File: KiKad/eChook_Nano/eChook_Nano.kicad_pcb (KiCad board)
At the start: 2 copper layers, 75 x 75 mm, 55 parts, among them J1 Expansion, Q1 BC547, U1 Arduino_Nano_v3.x, U2 TSR_1-2450, U3 MCP6002-xP

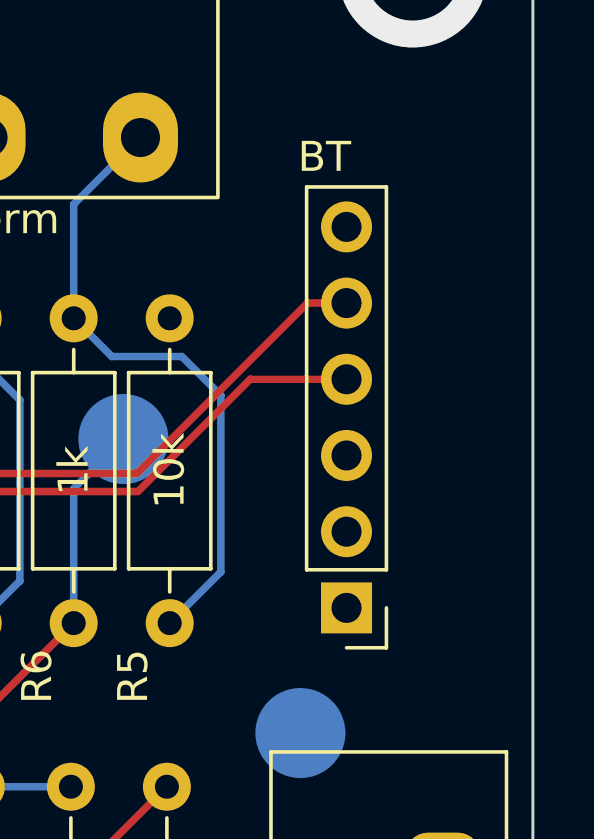
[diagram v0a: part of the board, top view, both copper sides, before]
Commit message: R15 and R24 Value Correction, new IBOM
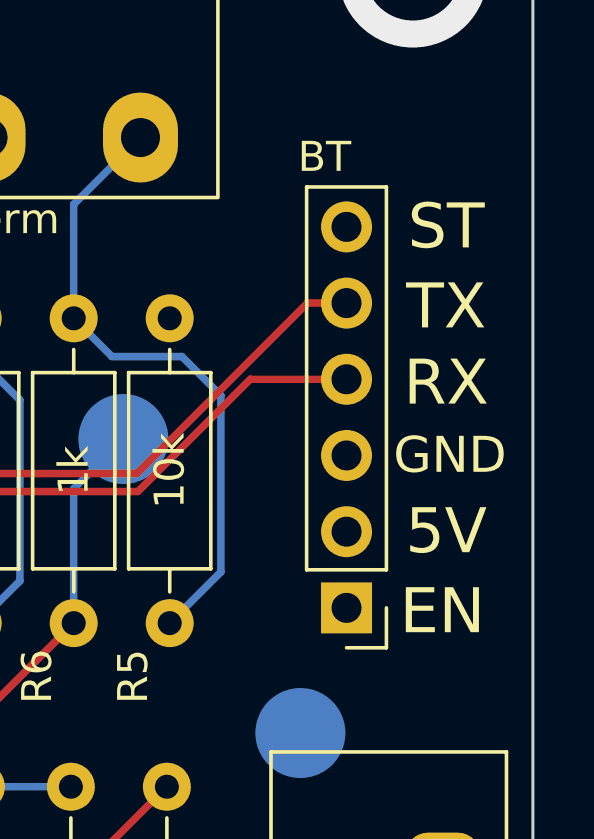
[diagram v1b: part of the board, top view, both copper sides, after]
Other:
- board text added: "5V"
- board text added: "EN"
- board text added: "RX"
- board text added: "ST"
- board text added: "TX"
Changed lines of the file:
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@@
     (effects (font (size 0.9 0.9) (thickness 0.225)) (justify mirror))
+  )
+  (gr_text "ST" (at 181.61 74.168) (layer "F.SilkS")
+    (effects (font (size 1.5 1.5) (thickness 0.3)))
+  )
+  (gr_text "GND" (at 181.737 81.788) (layer "F.SilkS")
+    (effects (font (size 1.2 1.2) (thickness 0.2)))
+  )
+  (gr_text "RX" (at 181.61 79.375) (layer "F.SilkS")
+    (effects (font (size 1.5 1.5) (thickness 0.3)))
   )
   (gr_text "8" (at 111.2 107.2) (layer "F.SilkS")
     (effects (font (size 1 1) (thickness 0.2)))
   )
+  (gr_text "EN" (at 181.483 86.995) (layer "F.SilkS")
+    (effects (font (size 1.5 1.5) (thickness 0.3)))
+  )
   (gr_text "1" (at 130.5 101.2) (layer "F.SilkS")
     (effects (font (size 1 1) (thickness 0.2)))
+  )
+  (gr_text "5V" (at 181.61 84.328) (layer "F.SilkS")
+    (effects (font (size 1.5 1.5) (thickness 0.3)))
+  )
+  (gr_text "TX" (at 181.61 76.835) (layer "F.SilkS")
+    (effects (font (size 1.5 1.5) (thickness 0.3)))
   )
   (gr_text "14\n" (at 130.5 107.2) (layer "F.SilkS")
@@
   (segment (start 120.3 100.8) (end 120.3 84.9) (width 0.25) (layer "F.Cu") (net 17))
   (segment (start 120.98 101.48) (end 120.3 100.8) (width 0.25) (layer "F.Cu") (net 17))
+  (segment (start 117.8 84.86) (end 119.07 83.59) (width 0.25) (layer "F.Cu") (net 18))
   (segment (start 118.44 102.8) (end 118.44 101.54) (width 0.25) (layer "F.Cu") (net 18))
-  (segment (start 117.8 84.86) (end 119.07 83.59) (width 0.25) (layer "F.Cu") (net 18))
   (segment (start 117.8 100.9) (end 117.8 84.86) (width 0.25) (layer "F.Cu") (net 18))
   (segment (start 118.44 101.54) (end 117.8 100.9) (width 0.25) (layer "F.Cu") (net 18))

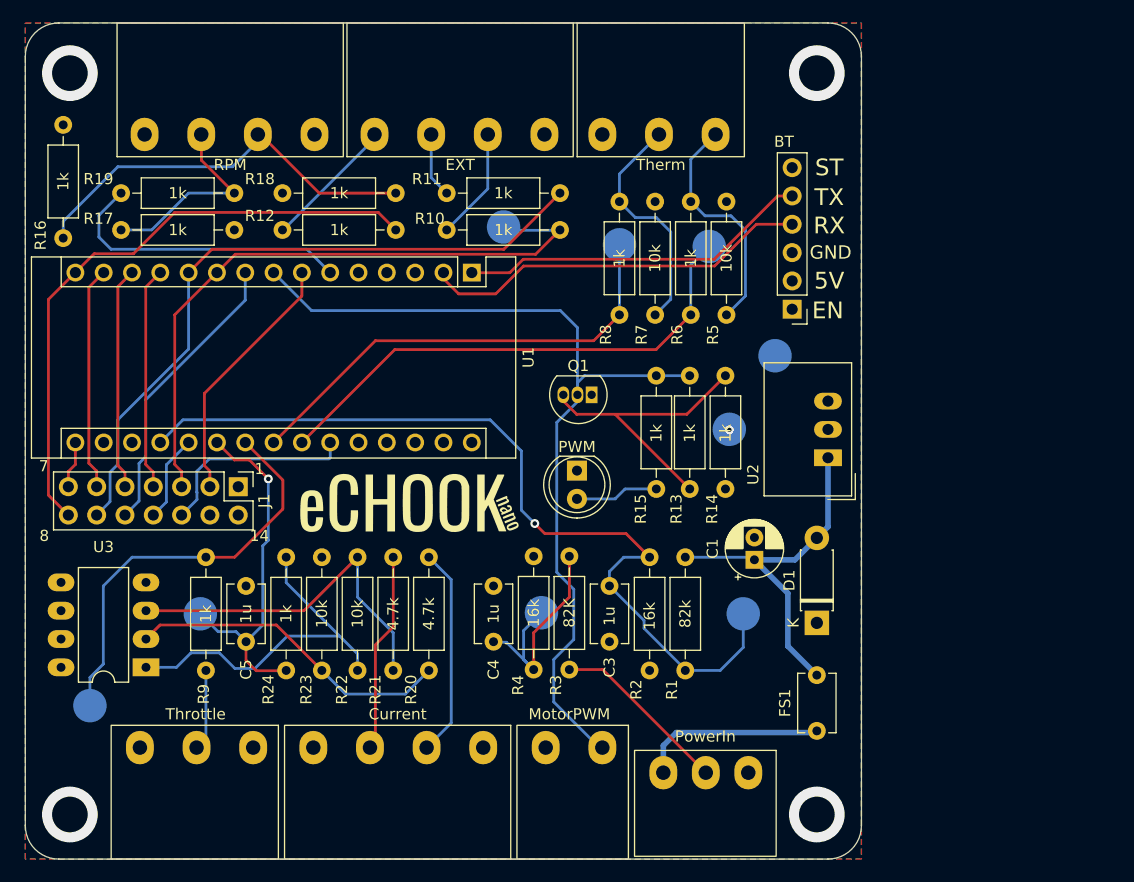
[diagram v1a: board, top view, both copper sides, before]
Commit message: SMD Conversion
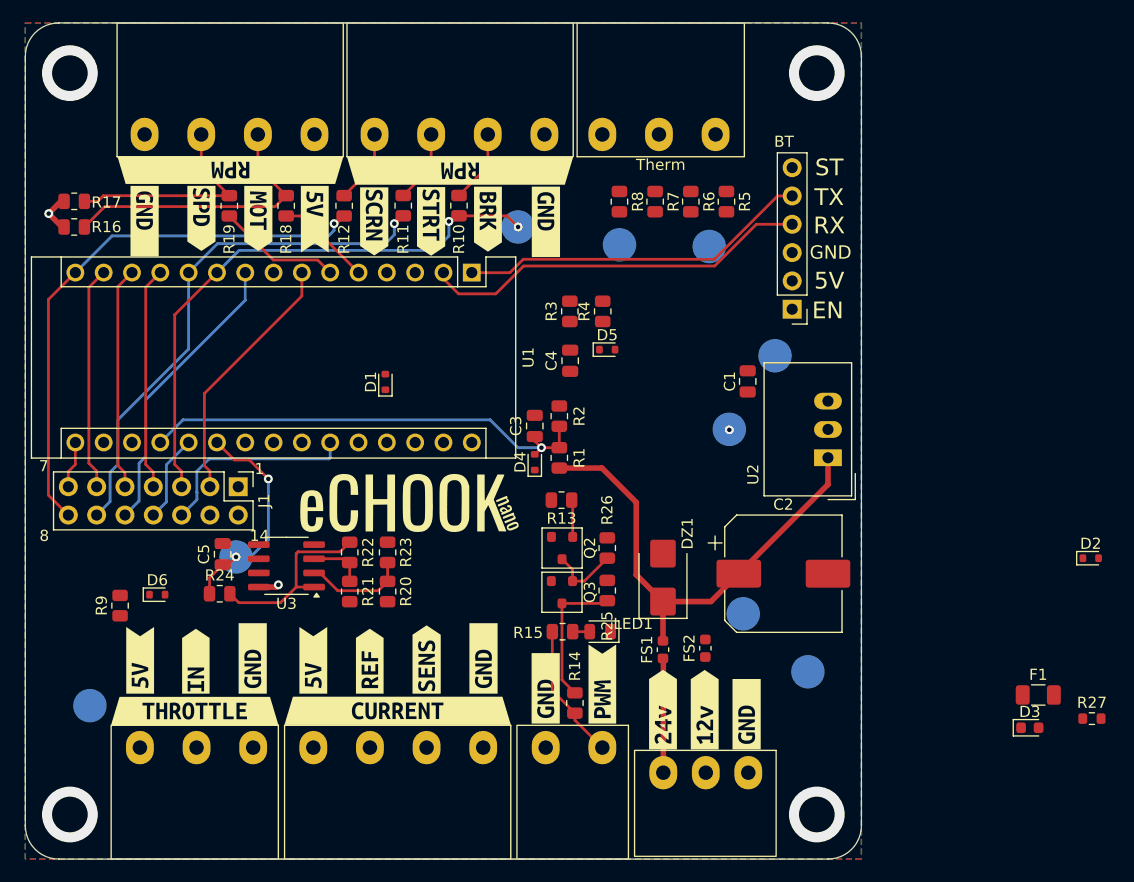
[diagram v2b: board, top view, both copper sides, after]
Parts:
- removed Q1: BC547, Package_TO_SOT_THT:TO-92L_Inline
- added C2: 47uf 63V, Capacitor_SMD:CP_Elec_10x10, F.Cu at (177.5, 110.6)
- added D2: SBD, Diode_SMD:D_SOD-523, F.Cu at (205.1, 109.2)
- added D3: LED, LED_SMD:LED_0603_1608Metric, F.Cu at (199.6, 124.4)
- added D4: SBD, Diode_SMD:D_SOD-523, F.Cu at (155.2, 100.6)
- added D5: SBD, Diode_SMD:D_SOD-523, F.Cu at (161.7, 90.5)
- added D6: SBD, Diode_SMD:D_SOD-523, F.Cu at (121.3, 112.5)
- added DZ1: 33v 35v 37v, Diode_SMD:D_SMB, F.Cu at (166.7, 111.0)
- added F1: Polyfuse, Fuse:Fuse_1206_3216Metric, F.Cu at (200.4, 121.5)
- added FS2: Polyfuse 300mA, Fuse:Fuse_0603_1608Metric, F.Cu at (170.5, 117.3)
- added Q2: Q_NMOS-D_Generic_GSD, PCM_Package_TO_SOT_SMD_AKL:SOT-23, F.Cu at (157.7, 108.3)
- added Q3: Q_NMOS-D_Generic_GSD, PCM_Package_TO_SOT_SMD_AKL:SOT-23, F.Cu at (157.6, 112.3)
- added R25: 10k, Resistor_SMD:R_0805_2012Metric, F.Cu at (161.7, 112.1)
- added R26: 10k, Resistor_SMD:R_0805_2012Metric, F.Cu at (161.7, 108.3)
- added R27: 3.3k 0.1%, Resistor_SMD:R_0603_1608Metric, F.Cu at (205.2, 123.6)
- added kibuzzard-66D71FF8: G***, kibuzzard-66D71FF8, F.Cu at (166.7, 122.8)
- added kibuzzard-66D7200F: G***, kibuzzard-66D7200F, F.Cu at (170.4, 122.8)
- added kibuzzard-66D72019: G***, kibuzzard-66D72019, F.Cu at (156.2, 79.0)
- added kibuzzard-66D72019: G***, kibuzzard-66D72019, F.Cu at (156.2, 120.9)
- added kibuzzard-66D72019: G***, kibuzzard-66D72019, F.Cu at (150.6, 118.2)
- added kibuzzard-66D72019: G***, kibuzzard-66D72019, F.Cu at (129.9, 118.2)
- added kibuzzard-66D72019: G***, kibuzzard-66D72019, F.Cu at (174.2, 123.2)
- added kibuzzard-66D72019: G***, kibuzzard-66D72019, F.Cu at (120.2, 79.0)
- added kibuzzard-66D72322: G***, kibuzzard-66D72322, F.Cu at (161.3, 120.5)
- added kibuzzard-66D72613: G***, kibuzzard-66D72613, F.Cu at (135.3, 118.4)
- added kibuzzard-66D72613: G***, kibuzzard-66D72613, F.Cu at (119.8, 118.4)
- added kibuzzard-66D72613: G***, kibuzzard-66D72613, F.Cu at (135.5, 78.8)
- added kibuzzard-66D727FC: G***, kibuzzard-66D727FC, F.Cu at (140.4, 118.4)
- added kibuzzard-66D7283F: G***, kibuzzard-66D7283F, F.Cu at (145.5, 118.3)
- added kibuzzard-66D728C6: G***, kibuzzard-66D728C6, F.Cu at (124.8, 118.5)
- added kibuzzard-66D728F7: G***, kibuzzard-66D728F7, F.Cu at (124.7, 122.9)
- added kibuzzard-66D72997: G***, kibuzzard-66D72997, F.Cu at (142.9, 122.9)
- added kibuzzard-66D72A35: G***, kibuzzard-66D72A35, F.Cu at (127.9, 74.4)
- added kibuzzard-66D72A35: G***, kibuzzard-66D72A35, F.Cu at (148.5, 74.5)
- added kibuzzard-66D72A68: G***, kibuzzard-66D72A68, F.Cu at (125.3, 78.7)
- added kibuzzard-66D72A7D: G***, kibuzzard-66D72A7D, F.Cu at (130.4, 78.7)
- added kibuzzard-66D72AFE: G***, kibuzzard-66D72AFE, F.Cu at (151.0, 78.8)
- added kibuzzard-66D72B0C: G***, kibuzzard-66D72B0C, F.Cu at (145.9, 79.0)
- added kibuzzard-66D72B26: G***, kibuzzard-66D72B26, F.Cu at (140.8, 79.0)
- C1: value C_Polarized -> 22u 10V; footprint Capacitor_THT:CP_Radial_D5.0mm_P2.00mm -> Capacitor_SMD:C_0805_2012Metric
- C3, C4, C5: footprint Capacitor_THT:C_Disc_D5.1mm_W3.2mm_P5.00mm -> Capacitor_SMD:C_0805_2012Metric
- D1: value DIODE -> SBD; footprint Diode_THT:D_DO-41_SOD81_P7.62mm_Horizontal -> Diode_SMD:D_SOD-523
- FS1: value Polyfuse -> Polyfuse 300mA; footprint Capacitor_THT:C_Disc_D5.1mm_W3.2mm_P5.00mm -> Fuse:Fuse_0603_1608Metric
- LED1: renamed from PWM1; value PWM -> LED_GREEN; footprint LED_THT:LED_D5.0mm -> LED_SMD:LED_0805_2012Metric
- R1, R10, R11, R12, R14, R18, R19, R2, R20, R21, R22, R23, R3, R4, R5, R6, R7, R8, R9: footprint Resistor_THT:R_Axial_DIN0207_L6.3mm_D2.5mm_P10.16mm_Horizontal -> Resistor_SMD:R_0805_2012Metric
- R13, R15, R16, R17, R24: value 1k -> 10k; footprint Resistor_THT:R_Axial_DIN0207_L6.3mm_D2.5mm_P10.16mm_Horizontal -> Resistor_SMD:R_0805_2012Metric
- U3: footprint Package_DIP:DIP-8_W7.62mm_LongPads -> Package_SO:SOIC-8_3.9x4.9mm_P1.27mm
- moved D1 44.3 mm to (141.8, 93.4)
- moved R4 32.7 mm to (161.3, 87.1)
- moved R3 32.1 mm to (158.3, 87.1)
- moved R14 31.1 mm to (158.8, 122.2), turned to 90 degrees
- moved C4 26.1 mm to (158.4, 91.5)
- moved TP2 24.5 mm to (179.7, 119.4)
- moved C1 16.0 mm to (174.3, 93.3), turned to -90 degrees
- moved C3 15.8 mm to (155.2, 97.3), turned to 90 degrees
- moved FS1 15.6 mm to (166.7, 117.4)
- moved U3 15.5 mm to (132.9, 109.9)
- moved R15 15.3 mm to (157.7, 115.8), turned to 180 degrees
- moved R2 15.0 mm to (157.4, 96.5), turned to 90 degrees
- moved R13 14.7 mm to (157.6, 104.0), turned to 180 degrees
- moved LED1 14.6 mm to (161.1, 115.8), turned to 180 degrees
- moved R1 14.4 mm to (157.4, 100.2), turned to 90 degrees
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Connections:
- C1 pad 1: +24V -> +5V
- Conn2 pad 2: +12V -> Net-(Conn2-Pin_2)
- Conn8 pad 2: /MotorPWM -> Net-(Conn8-Pin_2)
- D1 pad 1: GND -> +5V
- D1 pad 2: +24V -> /Temp2
- R13 pad 1: GND -> /MotorPWM
- R13 pad 2: Net-(Q1-Pad3) -> GND
- R14 pad 1: /MotorPWM -> Net-(Conn8-Pin_2)
- R14 pad 2: Net-(Q1-Pad3) -> Net-(Q3-D)
- R15 pad 2: /MotorPWM -> Net-(Conn8-Pin_2)
- R18 pad 1: /MotorRMP -> /MotorRPM
- R20 pad 1: Net-(R20-Pad1) -> Net-(U3A--)
- R23 pad 1: Net-(R20-Pad1) -> GND
- R23 pad 2: GND -> Net-(U3A--)
- U3 pad 2: Net-(R20-Pad1) -> Net-(U3A--)
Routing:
- net /MotorPWM: track 81.6 -> 3.34 mm
- net /Temp1: track 46.4 -> 0.00 mm
- net /Temp2: track 40.8 -> 0.00 mm
- net /Throttle: track 37.6 -> 0.00 mm
- net /BattTotalV: track 77.8 -> 41.7 mm
- net Net-(R20-Pad1): track 29.3 -> 0.00 mm
- net Net-(U3A-+): track 32.4 -> 5.03 mm
- net Net-(Q1-Pad3): track 25.9 -> 0.00 mm
- net /Batt1v: track 22.4 -> 0.00 mm
- net Net-(Conn3-Pin_2): track 21.2 -> 0.00 mm
- net Net-(Conn3-Pin_1): track 21.2 -> 0.00 mm
- net Net-(Conn1-Pin_3): track 18.8 -> 0.00 mm
- net Net-(Conn1-Pin_2): track 17.3 -> 0.00 mm
- net +12V: track 16.1 -> 0.00 mm
- net Net-(R22-Pad1): track 32.5 -> 16.7 mm
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
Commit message: Routing Complete
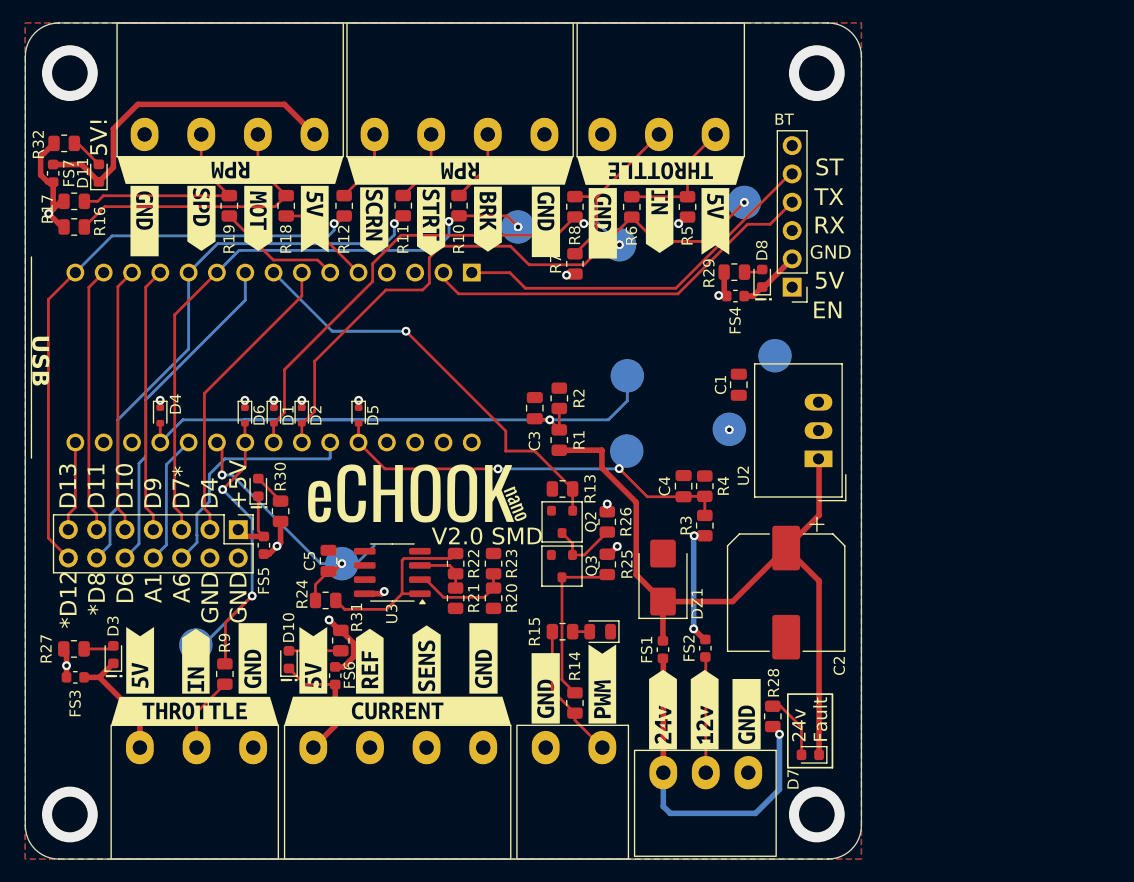
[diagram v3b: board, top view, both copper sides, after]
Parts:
- removed F1: Polyfuse, Fuse:Fuse_1206_3216Metric
- added BC1: BOM-Component, eChook:BOM-Component, F.Cu at (112.2, 83.7)
- added BC2: BOM-Component, eChook:BOM-Component, F.Cu at (112.2, 99.1)
- added D10: LED, LED_SMD:LED_0603_1608Metric, F.Cu at (133.2, 118.3)
- added D11: LED, LED_SMD:LED_0603_1608Metric, F.Cu at (116.1, 74.7)
- added D7: LED, LED_SMD:LED_0603_1608Metric, F.Cu at (179.9, 126.8)
- added D8: LED, LED_SMD:LED_0603_1608Metric, F.Cu at (175.6, 84.1)
- added D9: LED, LED_SMD:LED_0603_1608Metric, F.Cu at (130.4, 102.9)
- added FS3: Polyfuse 300mA, Fuse:Fuse_0603_1608Metric, F.Cu at (114.0, 119.9)
- added FS4: Polyfuse 300mA, Fuse:Fuse_0603_1608Metric, F.Cu at (173.2, 85.7)
- added FS5: Polyfuse 300mA, Fuse:Fuse_0603_1608Metric, F.Cu at (130.9, 108.0)
- added FS6: Polyfuse 300mA, Fuse:Fuse_0603_1608Metric, F.Cu at (137.3, 119.8)
- added FS7: Polyfuse 300mA, Fuse:Fuse_0603_1608Metric, F.Cu at (112.0, 74.7)
- added R28: 10k, Resistor_SMD:R_0805_2012Metric, F.Cu at (176.6, 123.4)
- added R29: 1k, Resistor_SMD:R_0805_2012Metric, F.Cu at (173.1, 83.5)
- added R30: 1k, Resistor_SMD:R_0805_2012Metric, F.Cu at (132.4, 105.0)
- added R31: 1k, Resistor_SMD:R_0805_2012Metric, F.Cu at (137.8, 116.6)
- added R32: 1k, Resistor_SMD:R_0805_2012Metric, F.Cu at (113.0, 72.0)
- added kibuzzard-66D72019: G***, kibuzzard-66D72019, F.Cu at (161.3, 79.2)
- added kibuzzard-66D72613: G***, kibuzzard-66D72613, F.Cu at (171.4, 79.0)
- added kibuzzard-66D728C6: G***, kibuzzard-66D728C6, F.Cu at (166.4, 78.9)
- added kibuzzard-66D728F7: G***, kibuzzard-66D728F7, F.Cu at (166.5, 74.5)
- R27: value 3.3k 0.1% -> 1k; footprint Resistor_SMD:R_0603_1608Metric -> Resistor_SMD:R_0805_2012Metric
- moved R27 91.5 mm to (113.9, 117.3), turned to 180 degrees
- moved D3 82.5 mm to (117.4, 117.9), turned to 90 degrees
- moved D2 71.9 mm to (134.3, 96.4), turned to -90 degrees
- moved G*** 67.6 mm to (79.9, 49.3)
- moved D4 33.9 mm to (121.6, 96.4), turned to -90 degrees
- moved TP2 25.6 mm to (163.4, 99.6)
- moved TP1 23.7 mm to (163.5, 92.8)
- moved D5 23.1 mm to (139.4, 96.4), turned to -90 degrees
- moved R3 22.7 mm to (170.4, 106.3)
- moved R4 18.2 mm to (170.4, 102.8)
- moved D6 17.9 mm to (129.2, 96.4), turned to -90 degrees
- moved C4 15.2 mm to (168.6, 102.8)
- moved R9 11.2 mm to (127.4, 119.6)
- moved TP8 10.9 mm to (124.8, 117.0)
- moved D1 10.4 mm to (131.8, 96.4), turned to -90 degrees
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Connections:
- net Net-(Conn2-Pin_1) renamed /24vIn
- Conn1 pad 1: +5V -> Net-(Conn1-Pin_1)
- Conn4 pad 1: +5V -> Net-(Conn4-Pin_1)
- Conn6 pad 1: +5V -> Net-(Conn6-Pin_1)
- Conn7 pad 2: +5V -> Net-(Conn7-Pin_2)
- D3 pad 1: /5V_Fused -> Net-(Conn6-Pin_1)
- J1 pad 1: +5V -> Net-(D9-K)
- U1 pad 26: /Batt1V -> /Batt1v
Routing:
- net /Temp1: track 0.00 -> 56.8 mm, vias 0 -> 1
- net /Temp2: track 0.00 -> 43.6 mm, vias 0 -> 2
- net /Batt1v: track 0.00 -> 36.8 mm, vias 0 -> 2
- net /MotorPWM: track 3.34 -> 37.9 mm, vias 0 -> 1
- net /BattTotalV: track 41.7 -> 74.8 mm
- net /Throttle: track 0.00 -> 31.4 mm, vias 0 -> 2
- net Net-(Conn4-Pin_1): track 0.00 -> 30.1 mm
- net +5V: track 5.77 -> 34.9 mm, vias 2 -> 15
- net +24V: track 43.1 -> 65.2 mm
- net /24vIn: track 10.3 -> 30.0 mm, vias 0 -> 1
- net Net-(Conn3-Pin_2): track 0.00 -> 16.0 mm
- net Net-(Conn3-Pin_1): track 0.00 -> 11.6 mm
- net Net-(Conn1-Pin_1): track 0.00 -> 11.2 mm
- net Net-(Conn6-Pin_1): track 0.00 -> 10.9 mm
- net +12V: track 0.00 -> 10.8 mm, vias 0 -> 2
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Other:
- board text added: "!"
- board text added: "*D12"
- board text added: "*D8"
- board text added: "24v Fault"
- board text added: "5V!"
- board text added: "A1"
- board text added: "A6"
- board text added: "D10"
- board text added: "D11"
- board text added: "D13"
- board text added: "D4"
- board text added: "D6"
- board text added: "D7*"
- board text added: "D9"
- board text added: "V2.0 SMD"
- board text removed: "14"
- board text removed: "7"
- board text removed: "8"
